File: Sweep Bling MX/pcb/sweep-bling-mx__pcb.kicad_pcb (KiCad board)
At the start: 2 copper layers, 113.5 x 95.2 mm, 31 parts, among them J2 AudioJack4dpb, SW10 SW_Push, SW11 SW_Push, SW12 SW_Push, SW14 SW_Push, SW15 SW_Push, SW16 SW_Push, SW17 SW_Push, SW18 SW_Push, SW2 SW_Push, SW20 SW_Push, SW21 SW_Push, SW3 SW_Push, SW4 SW_Push, SW5 SW_Push, SW6 SW_Push, SW8 SW_Push, SW9 SW_Push, U1 ProMicro-kbd

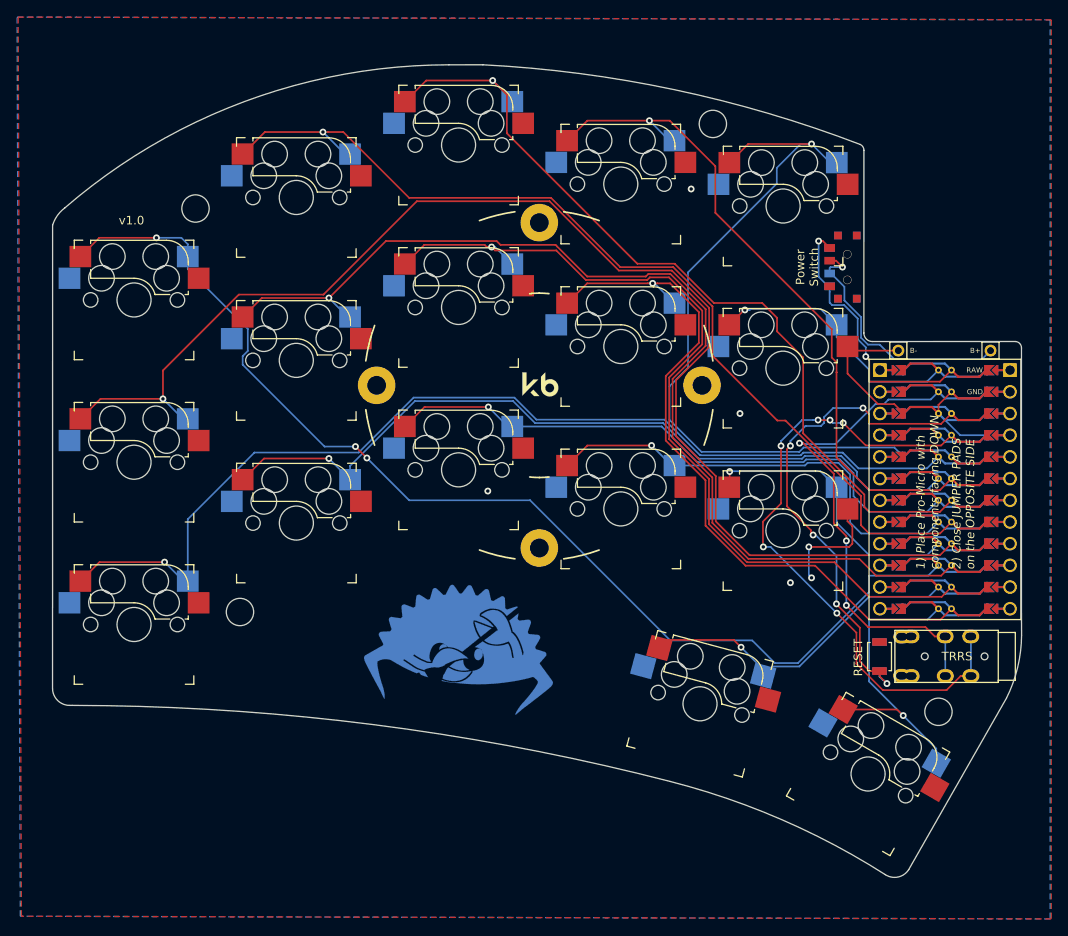
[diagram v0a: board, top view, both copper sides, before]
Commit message: Update Bling MX spacer hole diameter, silk & gerber
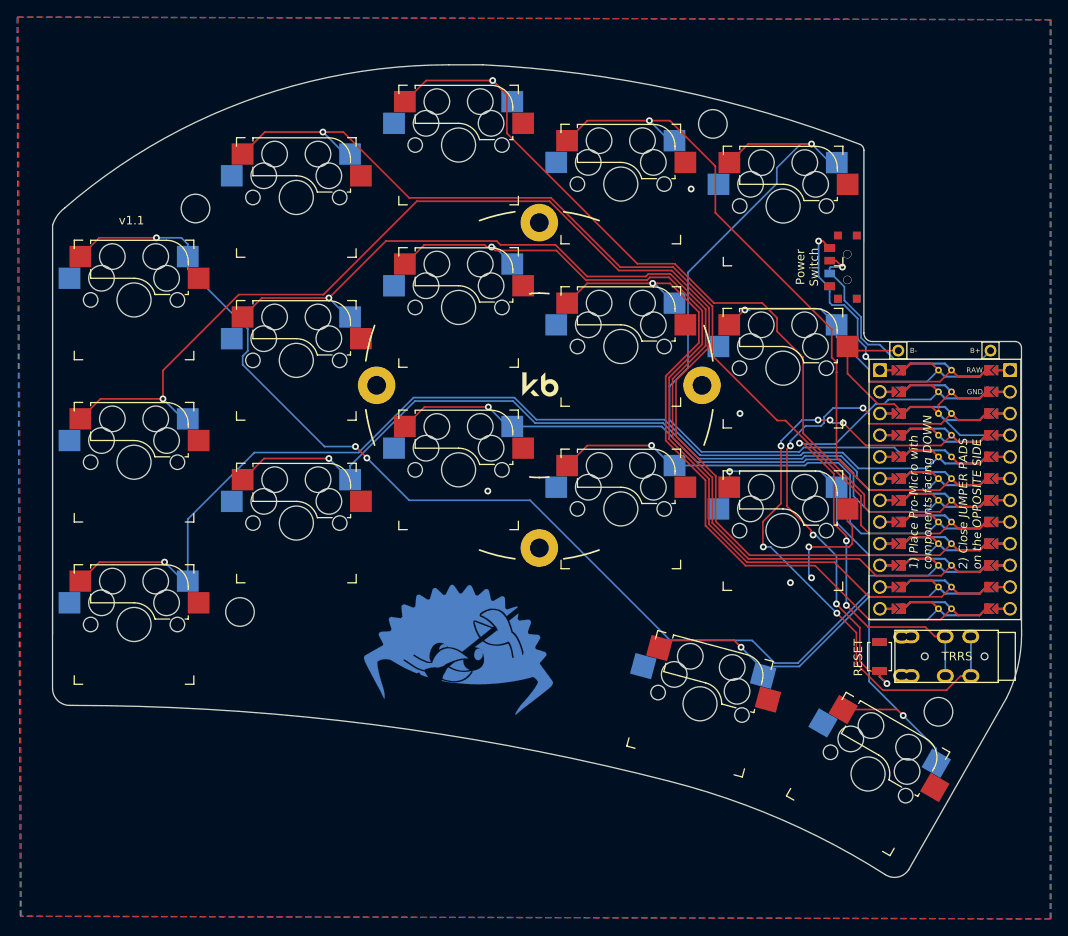
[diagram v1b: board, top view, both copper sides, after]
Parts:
- Mounting 01: value MountingHole_3.2mm_M3 -> MountingHole_3.35mm; footprint MountingHole:MountingHole_3.2mm_M3 -> duckyb-footprints:MountingHole_3.35mm
- Mounting 02: value MountingHole_3.2mm_M3 -> MountingHole_3.35mm; footprint MountingHole:MountingHole_3.2mm_M3 -> duckyb-footprints:MountingHole_3.35mm
- Mounting 03: value MountingHole_3.2mm_M3 -> MountingHole_3.35mm; footprint MountingHole:MountingHole_3.2mm_M3 -> duckyb-footprints:MountingHole_3.35mm
- Mounting 04: value MountingHole_3.2mm_M3 -> MountingHole_3.35mm; footprint MountingHole:MountingHole_3.2mm_M3 -> duckyb-footprints:MountingHole_3.35mm
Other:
- board text added: "v1.1"
- board text removed: "v1.0"
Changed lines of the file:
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@@
       (net 1 "gnd"))
   )
-  (footprint "MountingHole:MountingHole_3.2mm_M3" (layer "F.Cu")
+  (footprint "duckyb-footprints:MountingHole_3.35mm" (layer "F.Cu")
     (at 52.197 66.294)
     (descr "Mounting Hole 3.2mm, no annular, M3")
@@
       (effects (font (size 1 1) (thickness 0.15)))
     )
-    (fp_text value "MountingHole_3.2mm_M3" (at 0 4.2) (layer "F.Fab")
+    (fp_text value "MountingHole_3.35mm" (at 0 4.2) (layer "F.Fab")
       (effects (font (size 1 1) (thickness 0.15)))
     )
-    (fp_text user "${REFERENCE}" (at 0.3 0) (layer "F.Fab")
+    (fp_text user "${REFERENCE}" (at 0 0) (layer "F.Fab")
       (effects (font (size 1 1) (thickness 0.15)))
     )
     (fp_circle (center 0 0) (end 3.2 0) (layer "Cmts.User") (width 0.15) (fill none))
     (fp_circle (center 0 0) (end 3.45 0) (layer "F.CrtYd") (width 0.05) (fill none))
-    (pad "" np_thru_hole circle locked (at 0 0) (size 3.2 3.2) (drill 3.2) (layers *.Cu *.Mask))
+    (pad "" np_thru_hole circle (at 0 0) (size 3.35 3.35) (drill 3.35) (layers F&B.Cu *.Mask))
   )
-  (footprint "MountingHole:MountingHole_3.2mm_M3" (layer "F.Cu")
+  (footprint "duckyb-footprints:MountingHole_3.35mm" (layer "F.Cu")
     (at 57.404 113.538)
     (descr "Mounting Hole 3.2mm, no annular, M3")
@@
       (effects (font (size 1 1) (thickness 0.15)))
     )
-    (fp_text value "MountingHole_3.2mm_M3" (at 0 4.2) (layer "F.Fab")
+    (fp_text value "MountingHole_3.35mm" (at 0 4.2) (layer "F.Fab")
       (effects (font (size 1 1) (thickness 0.15)))
     )
-    (fp_text user "${REFERENCE}" (at 0.3 0) (layer "F.Fab")
+    (fp_text user "${REFERENCE}" (at 0 0) (layer "F.Fab")
       (effects (font (size 1 1) (thickness 0.15)))
     )
     (fp_circle (center 0 0) (end 3.2 0) (layer "Cmts.User") (width 0.15) (fill none))
     (fp_circle (center 0 0) (end 3.45 0) (layer "F.CrtYd") (width 0.05) (fill none))
-    (pad "" np_thru_hole circle locked (at 0 0) (size 3.2 3.2) (drill 3.2) (layers *.Cu *.Mask))
+    (pad "" np_thru_hole circle (at 0 0) (size 3.35 3.35) (drill 3.35) (layers F&B.Cu *.Mask))
   )
   (footprint "Kailh:SPDT_C128955r" (layer "F.Cu")
@@
       (net 22 "raw"))
   )
-  (footprint "MountingHole:MountingHole_3.2mm_M3" (layer "F.Cu")
+  (footprint "duckyb-footprints:MountingHole_3.35mm" (layer "F.Cu")
     (at 139.192 125.222)
     (descr "Mounting Hole 3.2mm, no annular, M3")
@@
       (effects (font (size 1 1) (thickness 0.15)))
     )
-    (fp_text value "MountingHole_3.2mm_M3" (at 0 4.2) (layer "F.Fab")
+    (fp_text value "MountingHole_3.35mm" (at 0 4.2) (layer "F.Fab")
       (effects (font (size 1 1) (thickness 0.15)))
     )
-    (fp_text user "${REFERENCE}" (at 0.3 0) (layer "F.Fab")
+    (fp_text user "${REFERENCE}" (at 0 0) (layer "F.Fab")
       (effects (font (size 1 1) (thickness 0.15)))
     )
     (fp_circle (center 0 0) (end 3.2 0) (layer "Cmts.User") (width 0.15) (fill none))
     (fp_circle (center 0 0) (end 3.45 0) (layer "F.CrtYd") (width 0.05) (fill none))
-    (pad "" np_thru_hole circle locked (at 0 0) (size 3.2 3.2) (drill 3.2) (layers *.Cu *.Mask))
+    (pad "" np_thru_hole circle (at 0 0) (size 3.35 3.35) (drill 3.35) (layers F&B.Cu *.Mask))
   )
-  (footprint "MountingHole:MountingHole_3.2mm_M3" (layer "F.Cu")
+  (footprint "duckyb-footprints:MountingHole_3.35mm" (layer "F.Cu")
     (at 112.776 56.388)
     (descr "Mounting Hole 3.2mm, no annular, M3")
@@
       (effects (font (size 1 1) (thickness 0.15)))
     )
-    (fp_text value "MountingHole_3.2mm_M3" (at 0 4.2) (layer "F.Fab")
+    (fp_text value "MountingHole_3.35mm" (at 0 4.2) (layer "F.Fab")
       (effects (font (size 1 1) (thickness 0.15)))
     )
-    (fp_text user "${REFERENCE}" (at 0.3 0) (layer "F.Fab")
+    (fp_text user "${REFERENCE}" (at 0 0) (layer "F.Fab")
       (effects (font (size 1 1) (thickness 0.15)))
     )
     (fp_circle (center 0 0) (end 3.2 0) (layer "Cmts.User") (width 0.15) (fill none))
     (fp_circle (center 0 0) (end 3.45 0) (layer "F.CrtYd") (width 0.05) (fill none))
-    (pad "" np_thru_hole circle locked (at 0 0) (size 3.2 3.2) (drill 3.2) (layers *.Cu *.Mask))
+    (pad "" np_thru_hole circle (at 0 0) (size 3.35 3.35) (drill 3.35) (layers F&B.Cu *.Mask))
   )
   (footprint "Kailh:SPDT_C128955" (layer "B.Cu")
@@
   (gr_line (start 85.843227 49.463504) (end 81.868 49.468) (layer "Edge.Cuts") (width 0.05))
   (gr_arc (start 36.893 66.223) (mid 57.870705 53.792798) (end 81.868 49.468) (layer "Edge.Cuts") (width 0.05))
-  (gr_text "1) Place Pro-Micro with\ncomponents facing DOWN" (at 137.922 89.281 90) (layer "B.SilkS")
+  (gr_text "1) Place Pro-Micro with\ncomponents facing DOWN" (at 137.102 89.281 90) (layer "B.SilkS")
     (effects (font (size 1 1) (thickness 0.15) italic) (justify left mirror))
   )
-  (gr_text "2) Close JUMPER PADS\non the OPPOSITE SIDE" (at 142.113 89.281 90) (layer "B.SilkS")
+  (gr_text "2) Close JUMPER PADS\non the OPPOSITE SIDE" (at 142.902 89.281 90) (layer "B.SilkS")
     (effects (font (size 1 1) (thickness 0.15) italic) (justify left mirror))
   )
@@
     (effects (font (size 0.6 0.6) (thickness 0.1)))
   )
-  (gr_text "1) Place Pro-Micro with\ncomponents facing DOWN" (at 137.922 108.585 90) (layer "F.SilkS")
+  (gr_text "1) Place Pro-Micro with\ncomponents facing DOWN" (at 137.102 108.585 90) (layer "F.SilkS")
     (effects (font (size 1 1) (thickness 0.15) italic) (justify left))
   )
-  (gr_text "v1.0" (at 44.704 67.691) (layer "F.SilkS")
+  (gr_text "v1.1" (at 44.704 67.691) (layer "F.SilkS")
     (effects (font (size 1 1) (thickness 0.15)))
   )
-  (gr_text "2) Close JUMPER PADS\non the OPPOSITE SIDE" (at 142.113 108.585 90) (layer "F.SilkS")
+  (gr_text "2) Close JUMPER PADS\non the OPPOSITE SIDE" (at 142.902 108.585 90) (layer "F.SilkS")
     (effects (font (size 1 1) (thickness 0.15) italic) (justify left))
   )
